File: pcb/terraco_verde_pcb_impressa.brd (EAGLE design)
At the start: 100.3 x 60.6 mm, 15 parts

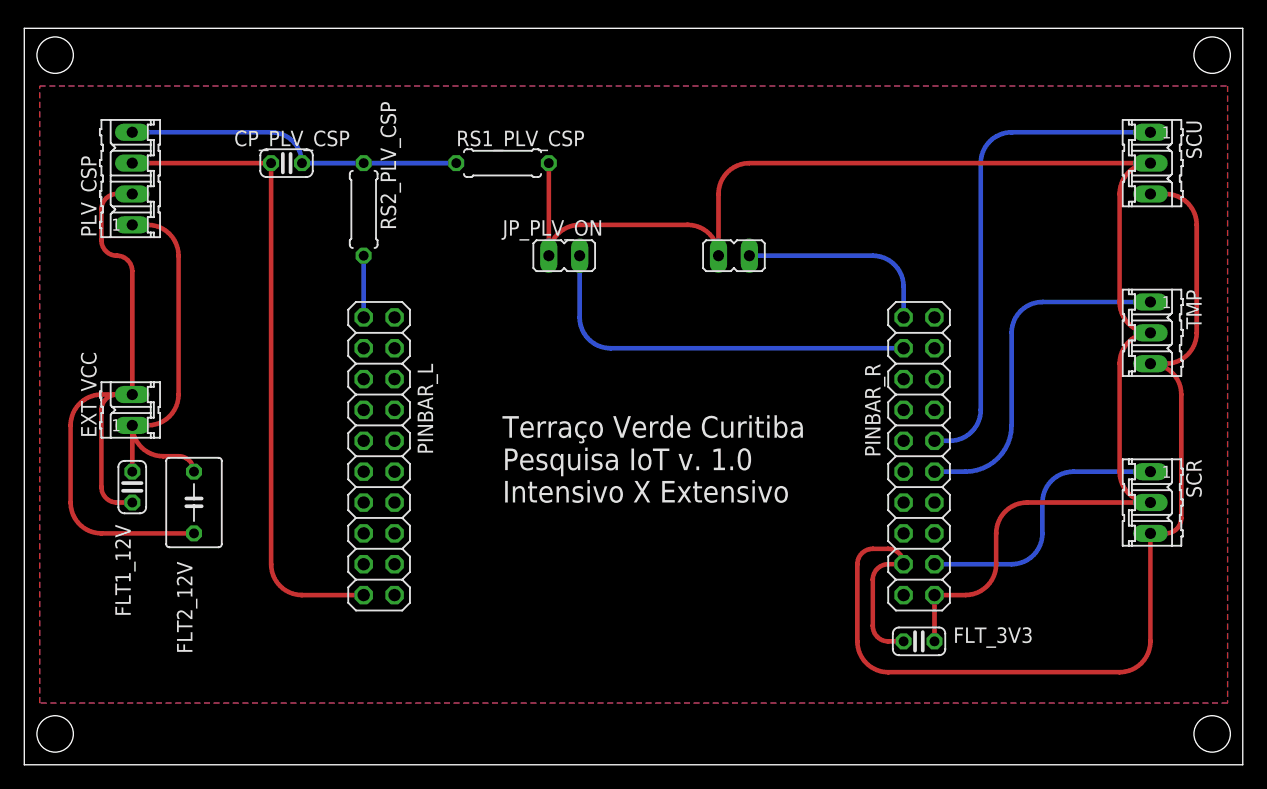
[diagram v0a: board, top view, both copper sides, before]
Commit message: Alteração no projeto da PCB para incluir plano de terra e vias.
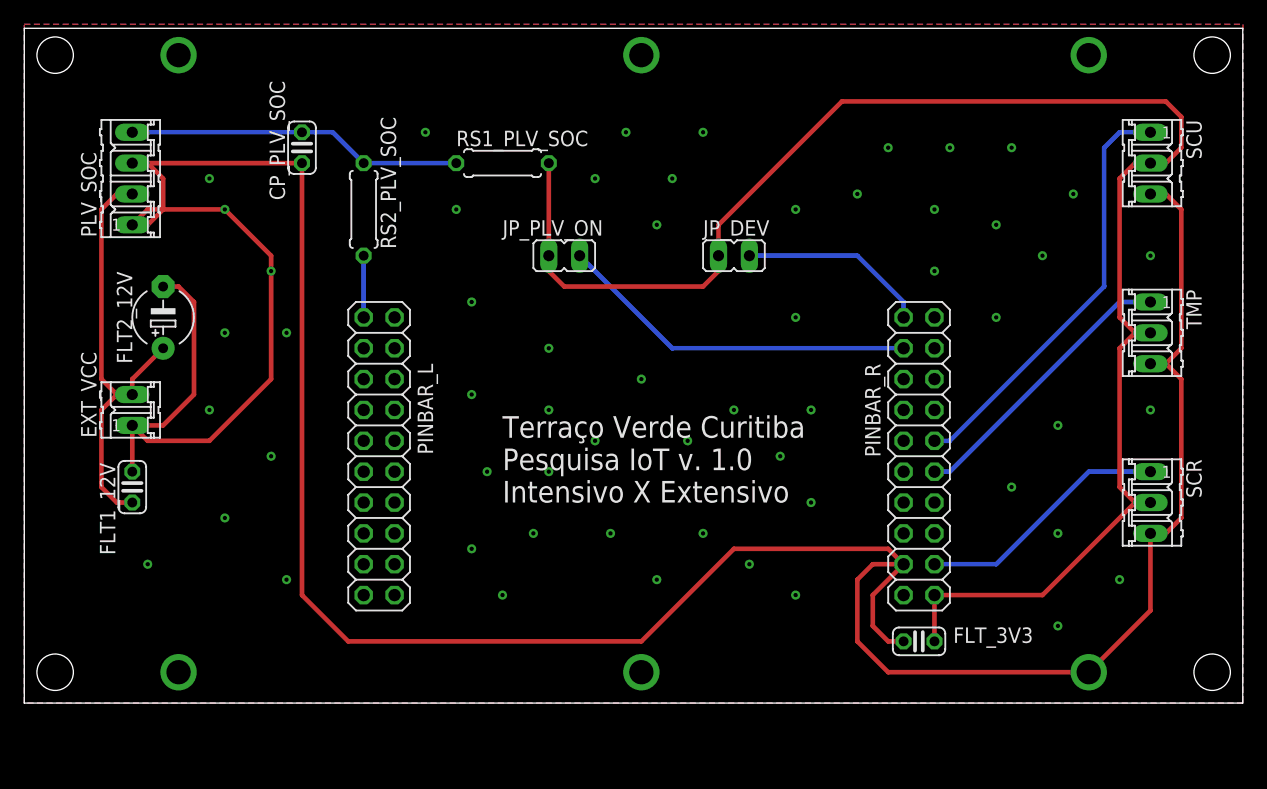
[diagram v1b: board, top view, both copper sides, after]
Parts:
- removed CP_PLV_CSP: 1KpF, rcl:C025-024X044
- added CP_PLV_SOC: 1KpF, rcl:C025-024X044
- FLT2_12V: device rcl:C050-045X075 -> rcl:E5-5
- moved FLT2_12V 15.5 mm to (36.8, 69.8)
- renumbered PLV_CSP to PLV_SOC, RS1_PLV_CSP to RS1_PLV_SOC, RS2_PLV_CSP to RS2_PLV_SOC
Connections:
- net N$1 renamed VCC_3V3
- net N$10 renamed NDI15
- net N$11 renamed NDI22
- net N$12 renamed NAI24
- net N$6 renamed NAI23
- net N$7 renamed NDI01
- net N$8 renamed NDI00
- removed net N$13: CP_PLV_CSP.2, PLV_SOC.4, RS1_PLV_SOC.1, RS2_PLV_SOC.1
- removed net N$2: FLT_3V3.2, PINBAR_R.17, SCR.3, SCU.3, TMP.3
- removed net N$3: EXT_VCC.1, FLT1_12V.2, FLT2_12V.2, PLV_SOC.1
- removed net N$4: CP_PLV_CSP.1, PINBAR_L.19, PLV_SOC.3
- removed net N$5: EXT_VCC.2, FLT1_12V.1, FLT2_12V.1, PLV_SOC.2
- new net GND: CP_PLV_SOC.1, EXT_VCC.1, FLT1_12V.2, FLT2_12V.-, FLT_3V3.2, PINBAR_R.17, PLV_SOC.1, PLV_SOC.3, SCR.3, SCU.3, TMP.3
- new net NDI15_2: CP_PLV_SOC.2, PLV_SOC.4, RS1_PLV_SOC.1, RS2_PLV_SOC.1
- new net VCC_12V: EXT_VCC.2, FLT1_12V.1, FLT2_12V.+, PLV_SOC.2
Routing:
- net GND: track 0.00 -> 257.5 mm, vias 0 -> 63
- net N$2: track 91.7 -> 0.00 mm
- net N$5: track 55.5 -> 0.00 mm
- net N$4: track 53.1 -> 0.00 mm
- net VCC_12V: track 0.00 -> 36.2 mm
- net N$3: track 31.6 -> 0.00 mm
- net N$13: track 27.7 -> 0.00 mm
- net NDI15_2: track 0.00 -> 27.7 mm
- net VCC_3V3: track 123.8 -> 133.5 mm
- net NAI24: track 40.2 -> 35.0 mm
- net NDI22: track 28.0 -> 23.6 mm
- net NDI00: track 32.8 -> 29.8 mm
- net NAI23: track 22.4 -> 20.9 mm
- net NDI01: track 16.3 -> 15.5 mm
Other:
- board size 100.3 x 60.6 mm -> 100.3 x 55.6 mm
